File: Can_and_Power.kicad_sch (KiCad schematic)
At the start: 11 parts, among them J1 776280-1, J2 776280-1, U1 ADM3057EBRWZ

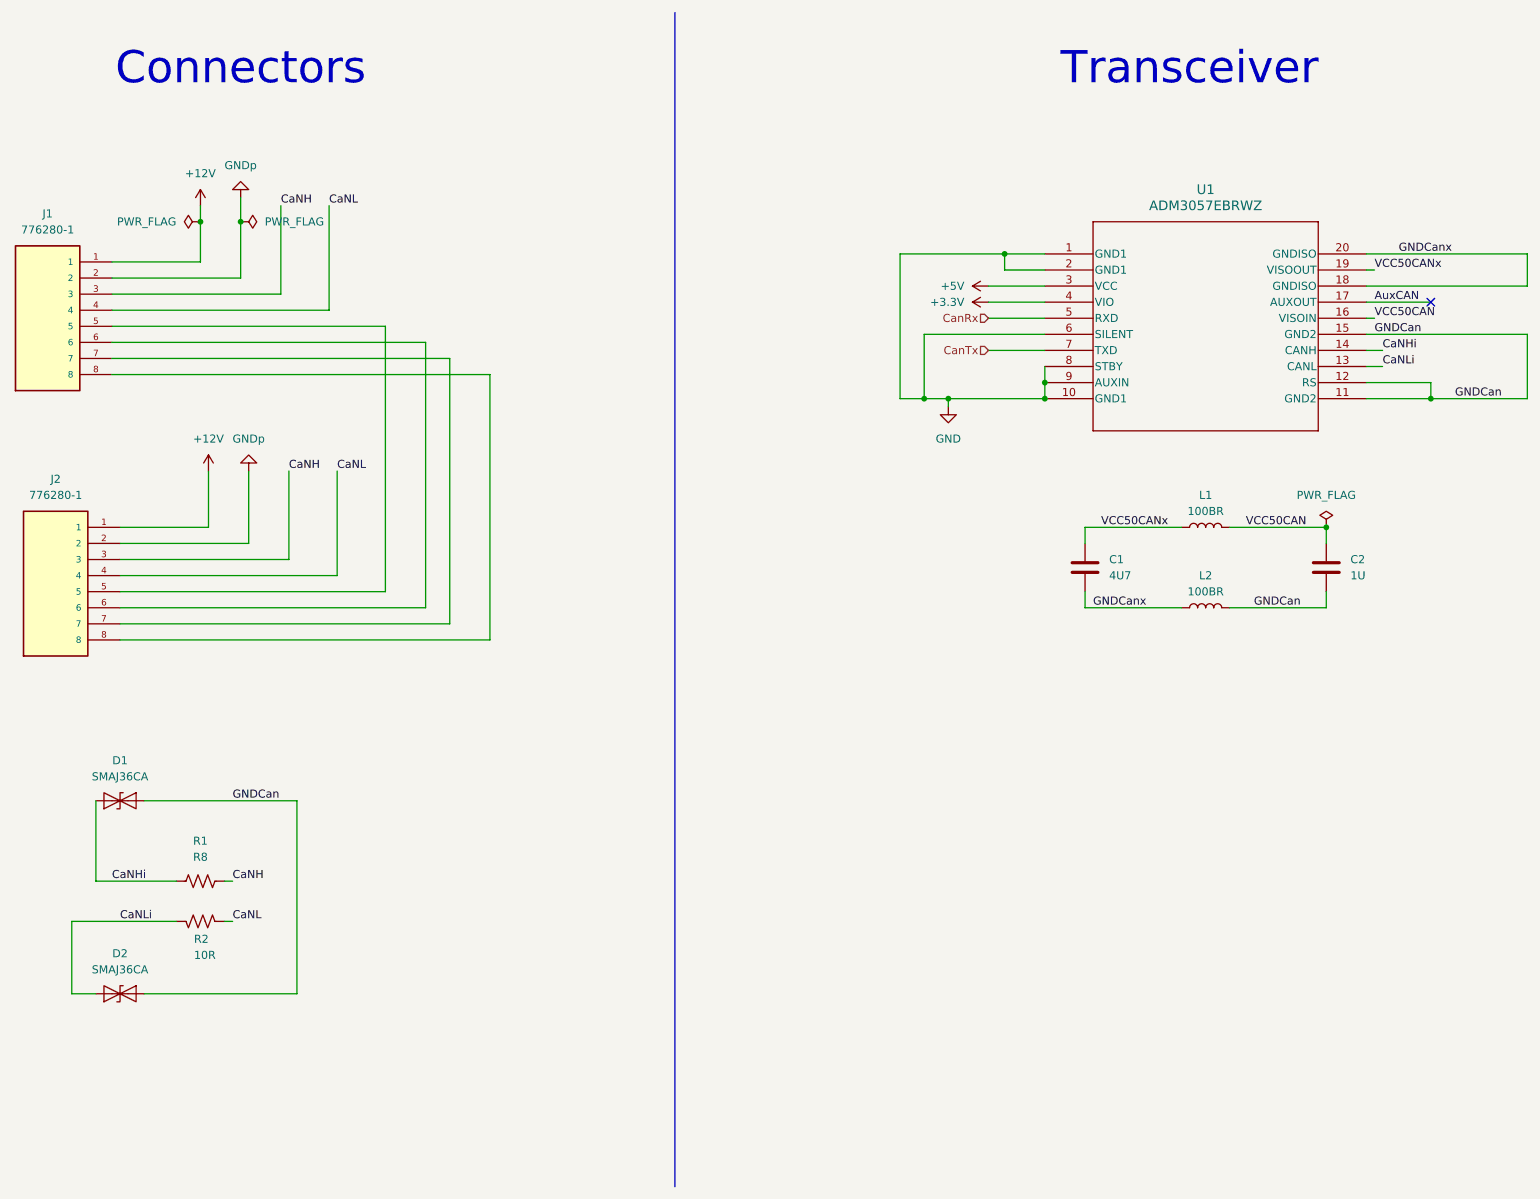
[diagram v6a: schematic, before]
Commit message: placed most components
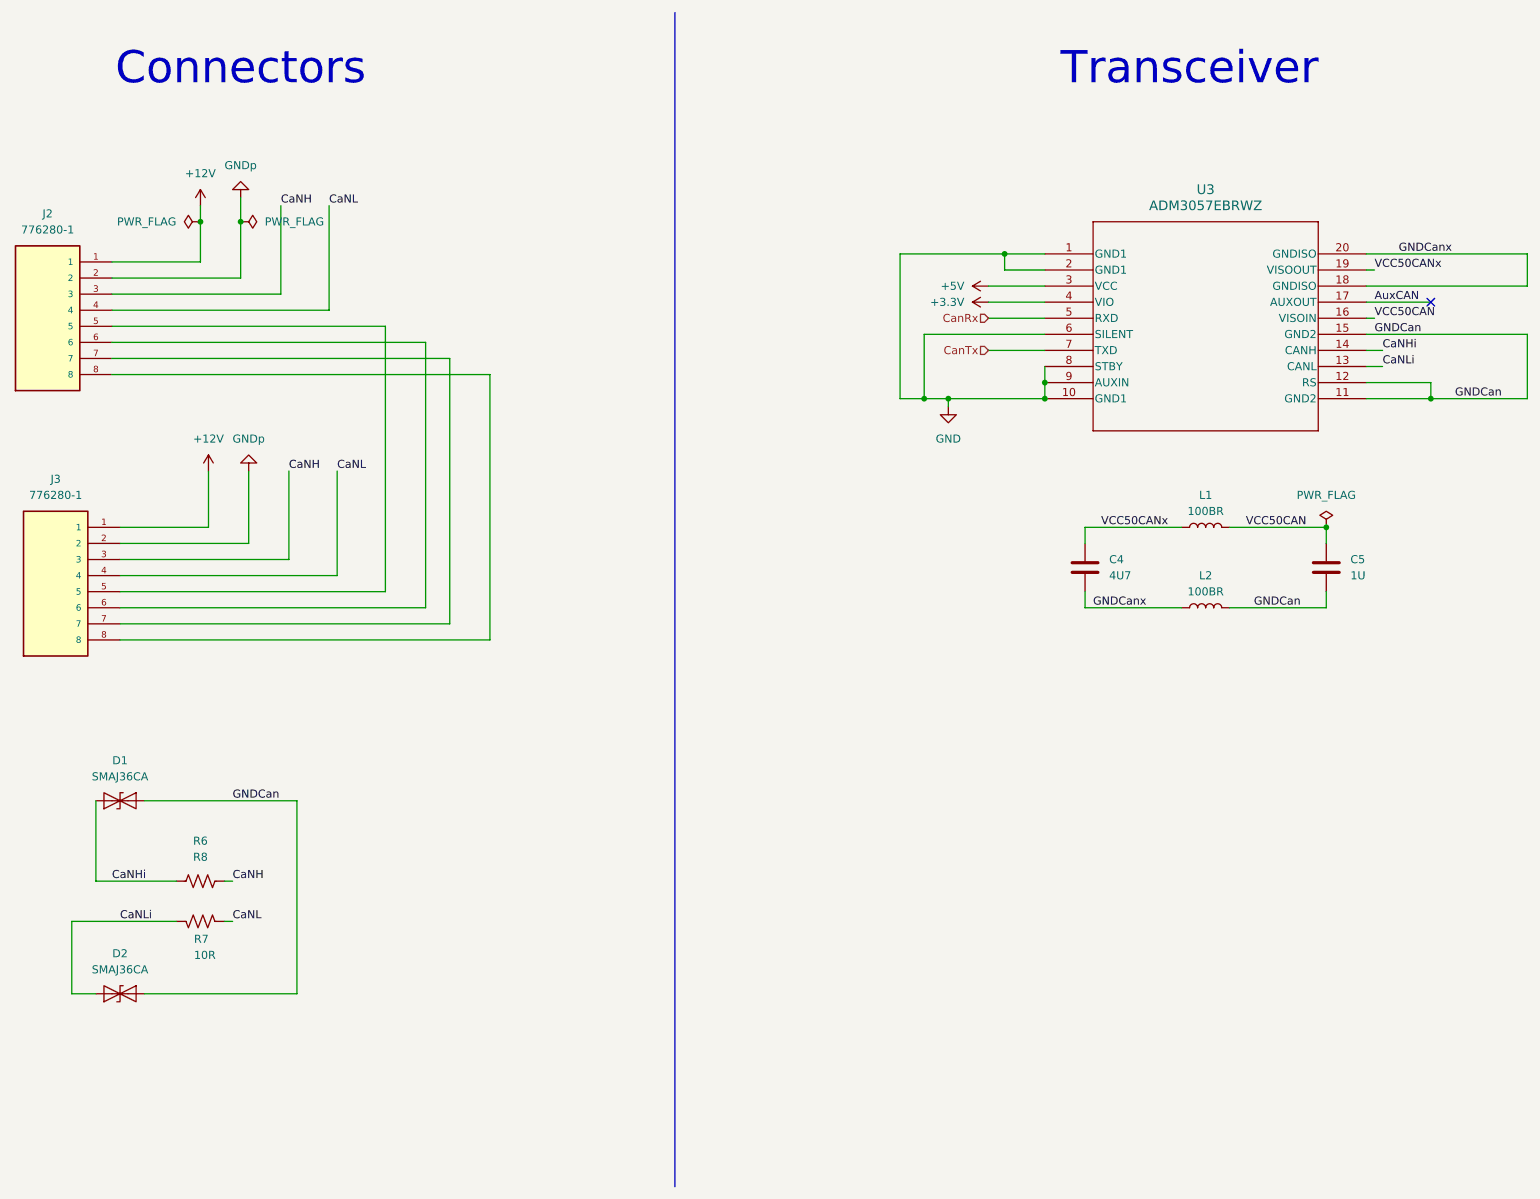
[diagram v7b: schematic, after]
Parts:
- R6: renamed from R1; footprint Resistor_SMD:R_0603_1608Metric -> Resistor_SMD:R_0805_2012Metric
- R7: renamed from R2; footprint Resistor_SMD:R_0603_1608Metric -> Resistor_SMD:R_0805_2012Metric
- renumbered C1 to C4, C2 to C5, J1 to J2, J2 to J3, U1 to U3
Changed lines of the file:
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@@
 		(dnp no)
 		(fields_autoplaced yes)
-		(property "Reference" "#PWR07"
+		(property "Reference" "#PWR022"
 			(at 189.23 58.42 0)
 			(effects
@@
 			(project "Main-Board-V2"
 				(path "/c01682a2-308a-4674-9b8f-80e441c05d08/2eeb5b34-c445-4914-b41b-f611e24c0c64"
-					(reference "#PWR07")
+					(reference "#PWR022")
 					(unit 1)
 				)
@@
 		(dnp no)
 		(fields_autoplaced yes)
-		(property "Reference" "#PWR01"
+		(property "Reference" "#PWR016"
 			(at 60.96 46.99 0)
 			(effects
@@
 			(project "Main-Board-V2"
 				(path "/c01682a2-308a-4674-9b8f-80e441c05d08/2eeb5b34-c445-4914-b41b-f611e24c0c64"
-					(reference "#PWR01")
+					(reference "#PWR016")
 					(unit 1)
 				)
@@
 		(dnp no)
 		(fields_autoplaced yes)
-		(property "Reference" "#PWR06"
+		(property "Reference" "#PWR021"
 			(at 189.23 55.88 0)
 			(effects
@@
 			(project "Main-Board-V2"
 				(path "/c01682a2-308a-4674-9b8f-80e441c05d08/2eeb5b34-c445-4914-b41b-f611e24c0c64"
-					(reference "#PWR06")
+					(reference "#PWR021")
 					(unit 1)
 				)
@@
 		(on_board yes)
 		(dnp no)
-		(property "Reference" "J1"
+		(property "Reference" "J2"
 			(at 36.83 44.45 0)
 			(effects
@@
 			(project "Main-Board-V2"
 				(path "/c01682a2-308a-4674-9b8f-80e441c05d08/2eeb5b34-c445-4914-b41b-f611e24c0c64"
-					(reference "J1")
+					(reference "J2")
 					(unit 1)
 				)
@@
 		(dnp no)
 		(fields_autoplaced yes)
-		(property "Reference" "C2"
+		(property "Reference" "C5"
 			(at 242.57 99.0599 0)
 			(effects
@@
 			(project "Main-Board-V2"
 				(path "/c01682a2-308a-4674-9b8f-80e441c05d08/2eeb5b34-c445-4914-b41b-f611e24c0c64"
-					(reference "C2")
+					(reference "C5")
 					(unit 1)
 				)
@@
 		(dnp no)
 		(fields_autoplaced yes)
-		(property "Reference" "R1"
+		(property "Reference" "R6"
 			(at 60.96 143.51 90)
 			(effects
@@
 			)
 		)
-		(property "Footprint" "Resistor_SMD:R_0603_1608Metric"
+		(property "Footprint" "Resistor_SMD:R_0805_2012Metric"
 			(at 61.214 148.844 90)
 			(effects
@@
 			(project "Main-Board-V2"
 				(path "/c01682a2-308a-4674-9b8f-80e441c05d08/2eeb5b34-c445-4914-b41b-f611e24c0c64"
-					(reference "R1")
+					(reference "R6")
 					(unit 1)
 				)
@@
 		(dnp no)
 		(fields_autoplaced yes)
-		(property "Reference" "#PWR03"
+		(property "Reference" "#PWR018"
 			(at 67.31 35.56 0)
 			(effects
@@
 			(project "Main-Board-V2"
 				(path "/c01682a2-308a-4674-9b8f-80e441c05d08/2eeb5b34-c445-4914-b41b-f611e24c0c64"
-					(reference "#PWR03")
+					(reference "#PWR018")
 					(unit 1)
 				)
@@
 		(on_board yes)
 		(dnp no)
-		(property "Reference" "J2"
+		(property "Reference" "J3"
 			(at 38.1 86.36 0)
 			(effects
@@
 			(project "Main-Board-V2"
 				(path "/c01682a2-308a-4674-9b8f-80e441c05d08/2eeb5b34-c445-4914-b41b-f611e24c0c64"
-					(reference "J2")
+					(reference "J3")
 					(unit 1)
 				)
@@
 		(dnp no)
 		(fields_autoplaced yes)
-		(property "Reference" "U1"
+		(property "Reference" "U3"
 			(at 219.71 40.64 0)
 			(effects
@@
 			(project "Main-Board-V2"
 				(path "/c01682a2-308a-4674-9b8f-80e441c05d08/2eeb5b34-c445-4914-b41b-f611e24c0c64"
-					(reference "U1")
+					(reference "U3")
 					(unit 1)
 				)
@@
 		(on_board yes)
 		(dnp no)
-		(property "Reference" "R2"
+		(property "Reference" "R7"
 			(at 59.944 159.004 90)
 			(effects
@@
 			)
 		)
-		(property "Footprint" "Resistor_SMD:R_0603_1608Metric"
+		(property "Footprint" "Resistor_SMD:R_0805_2012Metric"
 			(at 61.214 157.226 90)
 			(effects
@@
 			(project "Main-Board-V2"
 				(path "/c01682a2-308a-4674-9b8f-80e441c05d08/2eeb5b34-c445-4914-b41b-f611e24c0c64"
-					(reference "R2")
+					(reference "R7")
 					(unit 1)
 				)
@@
 		(dnp no)
 		(fields_autoplaced yes)
-		(property "Reference" "#PWR02"
+		(property "Reference" "#PWR017"
 			(at 62.23 88.9 0)
 			(effects
@@
 			(project "Main-Board-V2"
 				(path "/c01682a2-308a-4674-9b8f-80e441c05d08/2eeb5b34-c445-4914-b41b-f611e24c0c64"
-					(reference "#PWR02")
+					(reference "#PWR017")
 					(unit 1)
 				)
@@
 		(dnp no)
 		(fields_autoplaced yes)
-		(property "Reference" "#PWR04"
+		(property "Reference" "#PWR019"
 			(at 68.58 78.74 0)
 			(effects
@@
 			(project "Main-Board-V2"
 				(path "/c01682a2-308a-4674-9b8f-80e441c05d08/2eeb5b34-c445-4914-b41b-f611e24c0c64"
-					(reference "#PWR04")
+					(reference "#PWR019")
 					(unit 1)
 				)
@@
 		(dnp no)
 		(fields_autoplaced yes)
-		(property "Reference" "#PWR05"
+		(property "Reference" "#PWR020"
 			(at 179.07 81.28 0)
 			(effects
@@
 			(project "Main-Board-V2"
 				(path "/c01682a2-308a-4674-9b8f-80e441c05d08/2eeb5b34-c445-4914-b41b-f611e24c0c64"
-					(reference "#PWR05")
+					(reference "#PWR020")
 					(unit 1)
 				)
@@
 		(dnp no)
 		(fields_autoplaced yes)
-		(property "Reference" "C1"
+		(property "Reference" "C4"
 			(at 204.47 99.0599 0)
 			(effects
@@
 			(project "Main-Board-V2"
 				(path "/c01682a2-308a-4674-9b8f-80e441c05d08/2eeb5b34-c445-4914-b41b-f611e24c0c64"
-					(reference "C1")
-					(unit 1)
-				)
+					(reference "C4")
+					(unit 1)
+				)

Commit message: replaced CAN chip, power planes
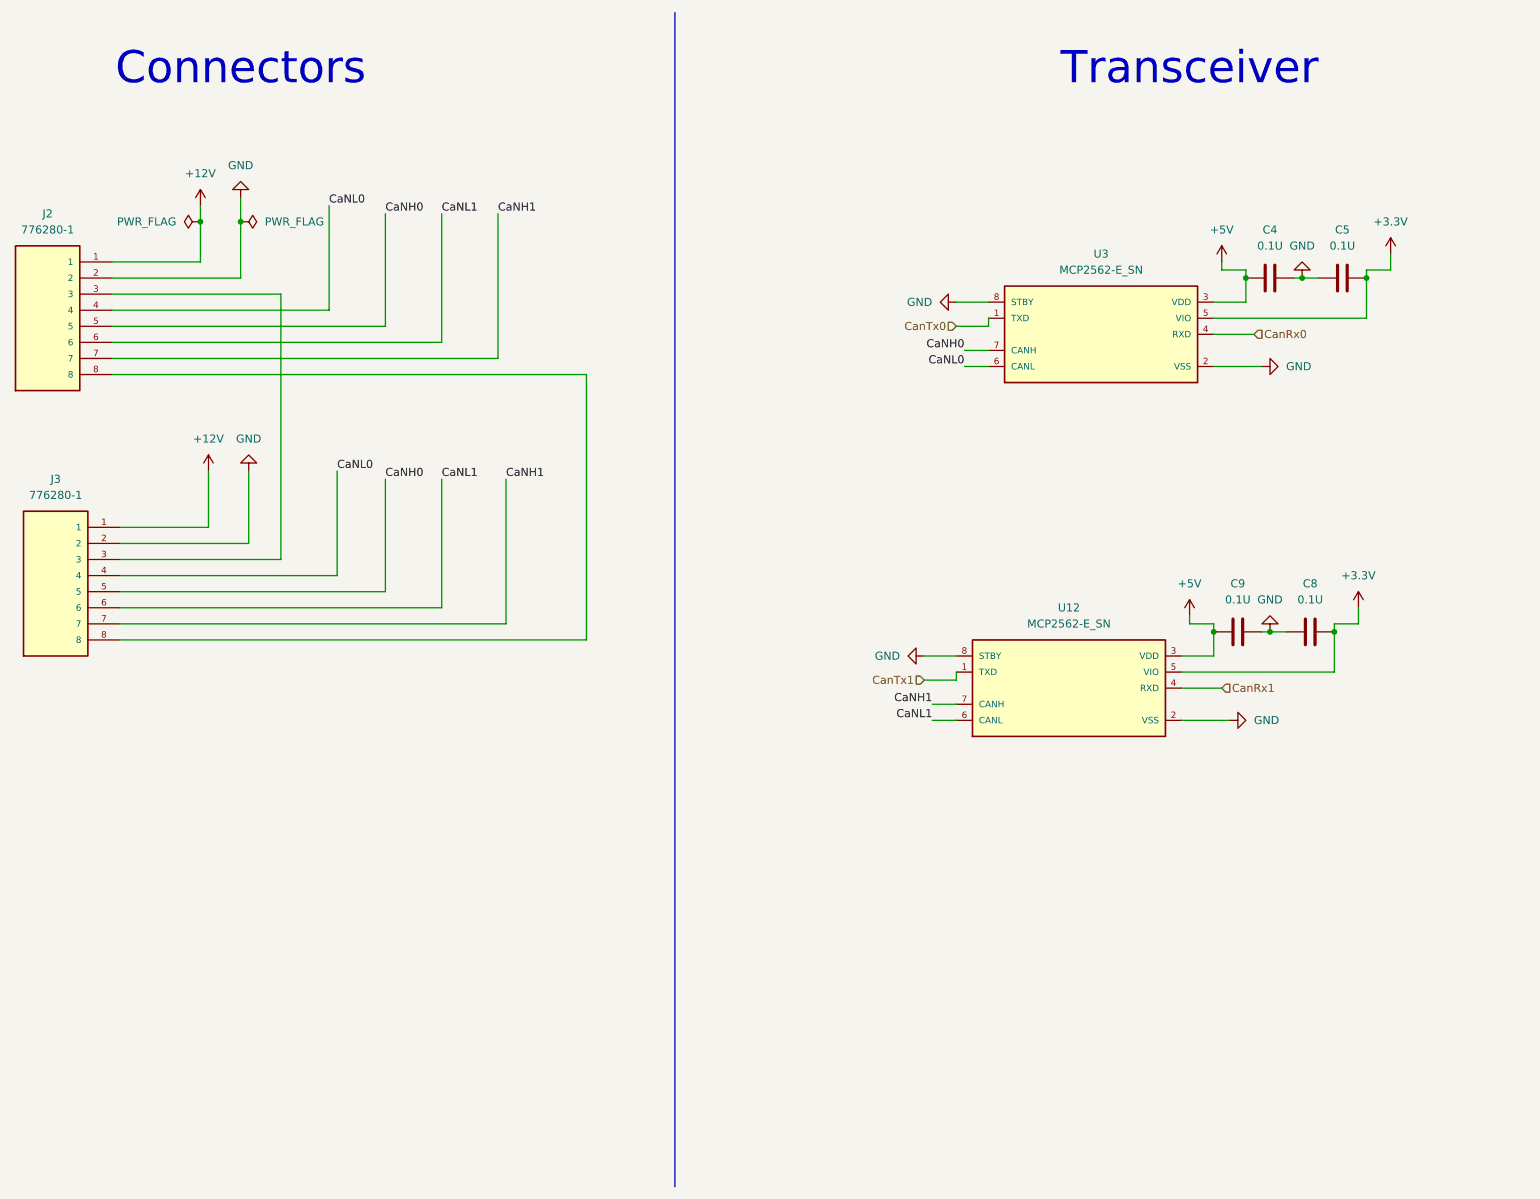
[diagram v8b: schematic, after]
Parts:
- removed D1, D2: SMAJ36CA, SMAJ36CA:SMASERIES-M, symbol Diode:SMAJ36CA
- removed L1, L2: 100BR, RN73C2B100RBTDF:RESC3015X65N, symbol Device:L
- removed R6: R8, Resistor_SMD:R_0805_2012Metric, symbol Device:R_US
- removed R7: 10R, Resistor_SMD:R_0805_2012Metric, symbol Device:R_US
- removed U3: ADM3057EBRWZ, ADM3057EBRWZ:SOIC127P1032X265-20N, symbol 2025-10-14_23-44-50:ADM3057EBRWZ
- added C8, C9: 0.1U, GRT155C80J105KE01J:CAPC1005X55N, symbol Device:C
- added U12, U3: MCP2562-E_SN, MCP2562-E_SN:SOIC127P600X175-8N, symbol MCP2562-E_SN:MCP2562-E_SN
- C4: value 4U7 -> 0.1U; footprint GRM188R61E475KE11D:CAPC1608X95N -> GRT155C80J105KE01J:CAPC1005X55N
- C5: value 1U -> 0.1U
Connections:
- net GNDCan is gone; now on net +3.3V: C5.2
- net GNDCanx is gone; now on net GND: C4.2
- net GNDp is gone; now on net GND: J2.2, J3.2
- net VCC50CAN is gone; now on net GND: C5.1
- net VCC50CANx is gone; now on net +5V: C4.1
- net +3.3V: now also C8.2, U12.5 (VIO), U3.5 (VIO)
- net +5V: now also C9.1, U12.3 (VDD), U3.3 (VDD)
- net GND: now also C8.1, C9.2, U12.2 (VSS), U12.8 (STBY), U3.2 (VSS), U3.8 (STBY)
- net CaNH0: now reaches J2.5, J3.5
- net CaNH0: now also U3.7 (CANH)
- net CaNL1: now reaches J2.6, J3.6
- net CaNL1: now also U12.6 (CANL)
- net CaNH1: now reaches J2.7, J3.7
- net CaNH1: now also U12.7 (CANH)
- net CaNH: no longer names the net of J2.3, J3.3
- net CaNL renamed CaNL0
- net CaNL0: now also U3.6 (CANL)
- new net CanRx0: U3.4 (RXD)
- new net CanRx1: U12.4 (RXD)
- new net CanTx0: U3.1 (TXD)
- new net CanTx1: U12.1 (TXD)
- no-connect marks 1 -> 0
